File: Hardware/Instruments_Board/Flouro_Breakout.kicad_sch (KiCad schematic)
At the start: 11 parts

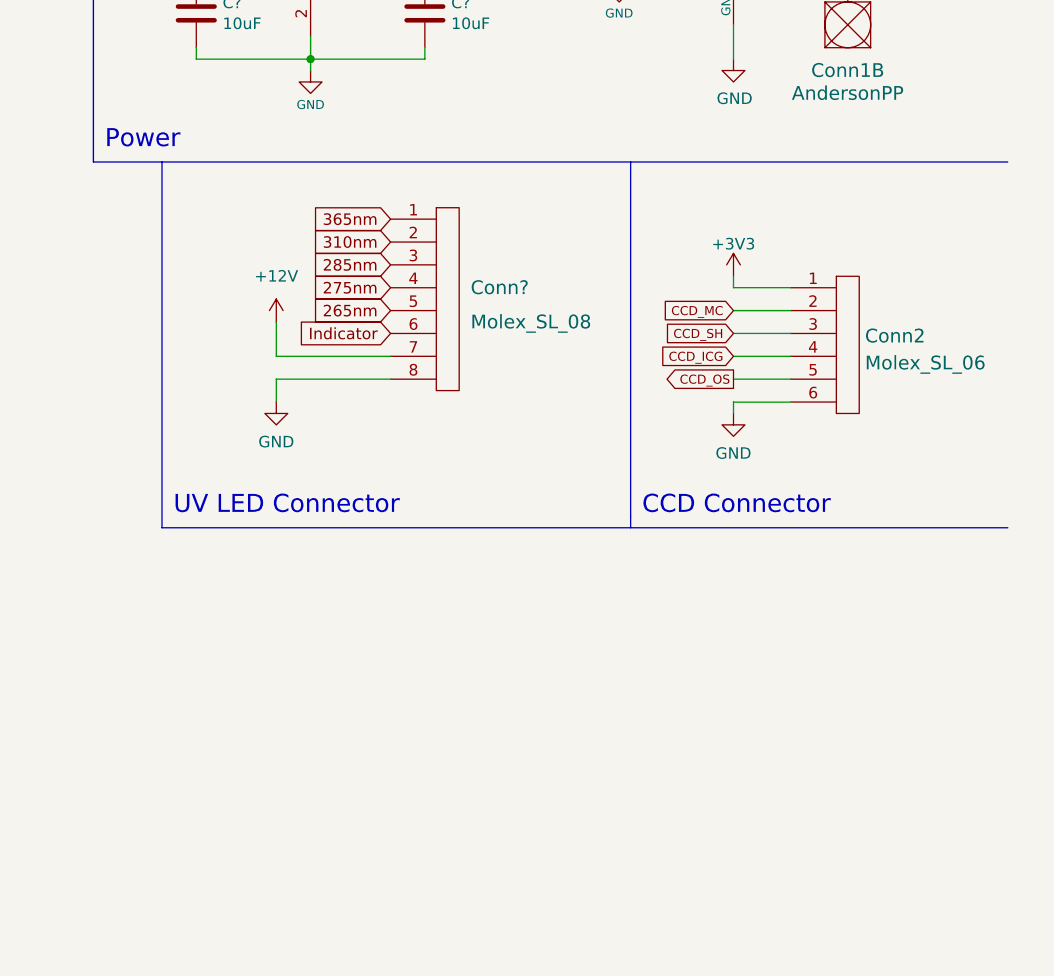
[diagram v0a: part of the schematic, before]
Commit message: New LED Footprints Made
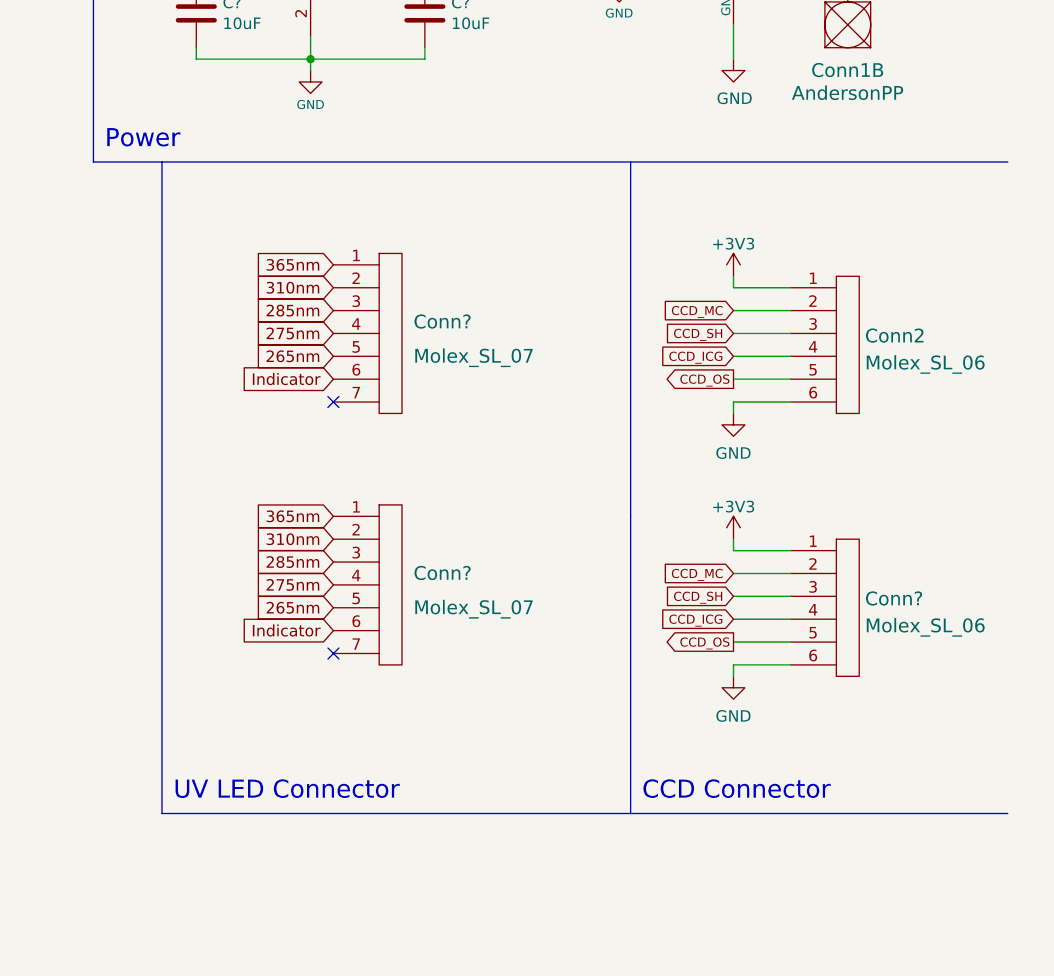
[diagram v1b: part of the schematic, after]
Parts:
- removed Conn?: Molex_SL_08, symbol MRDT_Connectors:Molex_SL_08
- added Conn? (x2): Molex_SL_07, symbol MRDT_Connectors:Molex_SL_07
- added Conn?: Molex_SL_06, Connector_Molex:Molex_SL_171971-0006_1x06_P2.54mm_Vertical, symbol Molex_SL_06:Molex_SL_06
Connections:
- net +3V3: now also Conn?.1
- net 265nm: now also Conn?.5, Conn?.5
- net 275nm: now also Conn?.4, Conn?.4
- net 285nm: now also Conn?.3, Conn?.3
- net 310nm: now also Conn?.2, Conn?.2
- net 365nm: now also Conn?.1, Conn?.1
- net CCD_ICG: now also Conn?.4
- net CCD_MC: now also Conn?.2
- net CCD_OS: now also Conn?.5
- net CCD_SH: now also Conn?.3
- net GND: now also Conn?.6
- net Indicator: now also Conn?.6, Conn?.6
- no-connect marks 3 -> 5

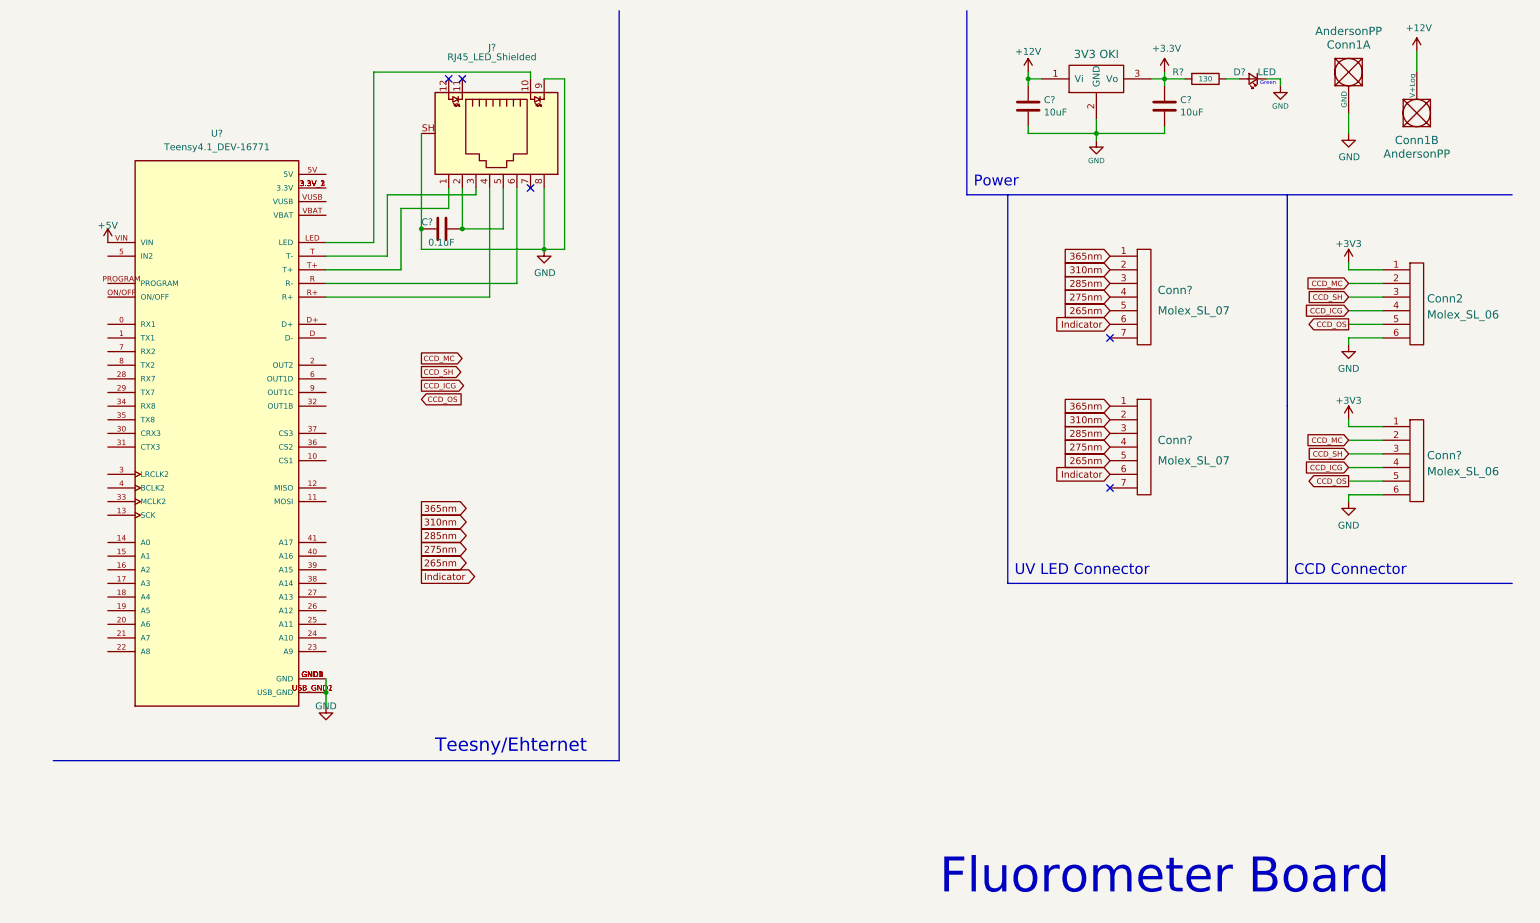
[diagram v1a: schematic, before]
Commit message: Began future proofing instruments board
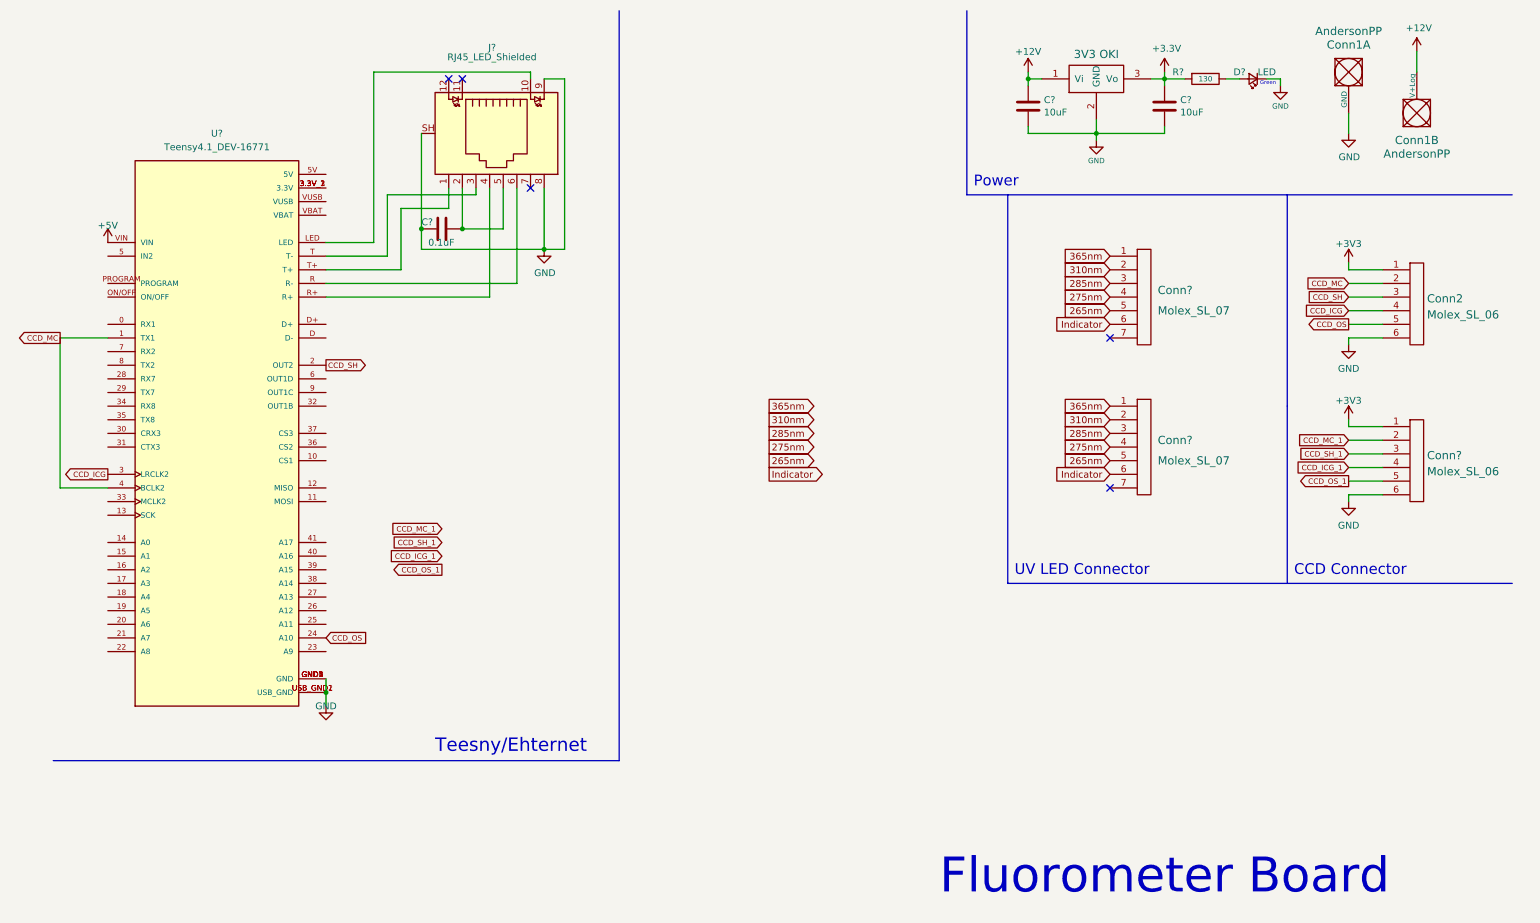
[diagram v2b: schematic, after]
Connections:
- net CCD_ICG: now also U?.3 (LRCLK2); no longer Conn?.4
- net CCD_MC: now also U?.1 (TX1), U?.4 (BCLK2); no longer Conn?.2
- net CCD_OS: now also U?.24 (A10); no longer Conn?.5
- net CCD_SH: now also U?.2 (OUT2); no longer Conn?.3
- new net  CCD_SH_1: Conn?.3
- new net CCD_ICG_1: Conn?.4
- new net CCD_MC_1: Conn?.2
- new net CCD_OS_1: Conn?.5
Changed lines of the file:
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@@
     (stroke (width 0) (type default) (color 0 0 0 0))
   )
+  (wire (pts (xy 13.97 101.6) (xy 22.86 101.6))
+    (stroke (width 0) (type default) (color 0 0 0 0))
+  )
   (wire (pts (xy 72.39 24.13) (xy 72.39 55.88))
     (stroke (width 0) (type default) (color 0 0 0 0))
@@
     (stroke (width 0) (type default) (color 0 0 0 0))
   )
+  (wire (pts (xy 22.86 73.66) (xy 13.97 73.66))
+    (stroke (width 0) (type default) (color 0 0 0 0))
+  )
   (wire (pts (xy 254 95.25) (xy 260.35 95.25))
     (stroke (width 0) (type default) (color 0 0 0 0))
@@
     (stroke (width 0) (type default) (color 0 0 0 0))
   )
+  (wire (pts (xy 13.97 73.66) (xy 13.97 101.6))
+    (stroke (width 0) (type default) (color 0 0 0 0))
+  )
   (wire (pts (xy 254 97.79) (xy 260.35 97.79))
     (stroke (width 0) (type default) (color 0 0 0 0))
@@
     (effects (font (size 2.5 2.5)) (justify left bottom))
   )
-  (global_label "Indicator" (shape output) (at 81.28 118.11 0) (fields_autoplaced)
+  (global_label "Indicator" (shape output) (at 146.05 99.06 0) (fields_autoplaced)
     (effects (font (size 1.27 1.27)) (justify left))
-    (property "Intersheet References" "${INTERSHEET_REFS}" (id 0) (at 92.0993 118.0306 0)
+    (property "Intersheet References" "${INTERSHEET_REFS}" (id 0) (at 156.8693 98.9806 0)
       (effects (font (size 1.27 1.27)) (justify left) hide)
     )
   )
+  (global_label "CCD_SH" (shape output) (at 63.5 78.74 0) (fields_autoplaced)
+    (effects (font (size 1 1)) (justify left))
+    (property "Intersheet References" "${INTERSHEET_REFS}" (id 0) (at 71.1619 78.6775 0)
+      (effects (font (size 1 1)) (justify left) hide)
+    )
+  )
+  (global_label "CCD_OS_1" (shape output) (at 85.09 116.84 180) (fields_autoplaced)
+    (effects (font (size 1 1)) (justify right))
+    (property "Intersheet References" "${INTERSHEET_REFS}" (id 0) (at 75.7138 116.7775 0)
+      (effects (font (size 1 1)) (justify right) hide)
+    )
+  )
   (global_label "CCD_OS" (shape output) (at 254 71.12 180) (fields_autoplaced)
     (effects (font (size 1 1)) (justify right))
@@
     )
   )
-  (global_label "265nm" (shape output) (at 81.28 115.57 0) (fields_autoplaced)
+  (global_label "265nm" (shape output) (at 146.05 96.52 0) (fields_autoplaced)
     (effects (font (size 1.27 1.27)) (justify left))
-    (property "Intersheet References" "${INTERSHEET_REFS}" (id 0) (at 90.1641 115.4906 0)
+    (property "Intersheet References" "${INTERSHEET_REFS}" (id 0) (at 154.9341 96.4406 0)
       (effects (font (size 1.27 1.27)) (justify left) hide)
     )
   )
-  (global_label "CCD_SH" (shape output) (at 81.28 80.01 0) (fields_autoplaced)
-    (effects (font (size 1 1)) (justify left))
-    (property "Intersheet References" "${INTERSHEET_REFS}" (id 0) (at 88.9419 79.9475 0)
-      (effects (font (size 1 1)) (justify left) hide)
-    )
-  )
   (global_label "265nm" (shape input) (at 209.55 96.52 180) (fields_autoplaced)
     (effects (font (size 1.27 1.27)) (justify right))
@@
     )
   )
-  (global_label "CCD_ICG" (shape input) (at 254 97.79 180) (fields_autoplaced)
+  (global_label "CCD_ICG_1" (shape input) (at 254 97.79 180) (fields_autoplaced)
+    (effects (font (size 1 1)) (justify right))
+    (property "Intersheet References" "${INTERSHEET_REFS}" (id 0) (at 244.1476 97.7275 0)
+      (effects (font (size 1 1)) (justify right) hide)
+    )
+  )
+  (global_label "CCD_MC_1" (shape input) (at 254 92.71 180) (fields_autoplaced)
     (effects (font (size 1 1)) (justify right))
-    (property "Intersheet References" "${INTERSHEET_REFS}" (id 0) (at 245.9319 97.7275 0)
+    (property "Intersheet References" "${INTERSHEET_REFS}" (id 0) (at 244.481 92.6475 0)
       (effects (font (size 1 1)) (justify right) hide)
     )
   )
-  (global_label "CCD_MC" (shape input) (at 254 92.71 180) (fields_autoplaced)
+  (global_label "CCD_MC" (shape output) (at 13.97 73.66 180) (fields_autoplaced)
     (effects (font (size 1 1)) (justify right))
-    (property "Intersheet References" "${INTERSHEET_REFS}" (id 0) (at 246.2652 92.6475 0)
+    (property "Intersheet References" "${INTERSHEET_REFS}" (id 0) (at 6.1652 73.7225 0)
       (effects (font (size 1 1)) (justify right) hide)
     )
   )
-  (global_label "285nm" (shape output) (at 81.28 110.49 0) (fields_autoplaced)
+  (global_label "285nm" (shape output) (at 146.05 91.44 0) (fields_autoplaced)
     (effects (font (size 1.27 1.27)) (justify left))
-    (property "Intersheet References" "${INTERSHEET_REFS}" (id 0) (at 90.1641 110.4106 0)
+    (property "Intersheet References" "${INTERSHEET_REFS}" (id 0) (at 154.9341 91.3606 0)
       (effects (font (size 1.27 1.27)) (justify left) hide)
     )
@@
     )
   )
-  (global_label "CCD_MC" (shape output) (at 81.28 77.47 0) (fields_autoplaced)
-    (effects (font (size 1 1)) (justify left))
-    (property "Intersheet References" "${INTERSHEET_REFS}" (id 0) (at 89.0848 77.4075 0)
-      (effects (font (size 1 1)) (justify left) hide)
+  (global_label " CCD_SH_1" (shape input) (at 85.09 111.76 180) (fields_autoplaced)
+    (effects (font (size 1 1)) (justify right))
+    (property "Intersheet References" "${INTERSHEET_REFS}" (id 0) (at 74.9519 111.6975 0)
+      (effects (font (size 1 1)) (justify right) hide)
     )
   )
@@
     )
   )
-  (global_label "365nm" (shape output) (at 81.28 105.41 0) (fields_autoplaced)
+  (global_label "365nm" (shape output) (at 146.05 86.36 0) (fields_autoplaced)
     (effects (font (size 1.27 1.27)) (justify left))
-    (property "Intersheet References" "${INTERSHEET_REFS}" (id 0) (at 90.1641 105.3306 0)
+    (property "Intersheet References" "${INTERSHEET_REFS}" (id 0) (at 154.9341 86.2806 0)
       (effects (font (size 1.27 1.27)) (justify left) hide)
     )
@@
     )
   )
-  (global_label "CCD_OS" (shape input) (at 81.28 85.09 0) (fields_autoplaced)
-    (effects (font (size 1 1)) (justify left))
-    (property "Intersheet References" "${INTERSHEET_REFS}" (id 0) (at 88.9419 85.0275 0)
-      (effects (font (size 1 1)) (justify left) hide)
-    )
-  )
   (global_label "Indicator" (shape input) (at 209.55 99.06 180) (fields_autoplaced)
     (effects (font (size 1.27 1.27)) (justify right))
@@
     )
   )
+  (global_label "CCD_MC_1" (shape input) (at 85.09 109.22 180) (fields_autoplaced)
+    (effects (font (size 1 1)) (justify right))
+    (property "Intersheet References" "${INTERSHEET_REFS}" (id 0) (at 75.571 109.1575 0)
+      (effects (font (size 1 1)) (justify right) hide)
+    )
+  )
   (global_label "365nm" (shape input) (at 209.55 86.36 180) (fields_autoplaced)
     (effects (font (size 1.27 1.27)) (justify right))
@@
     )
   )
-  (global_label "CCD_ICG" (shape output) (at 81.28 82.55 0) (fields_autoplaced)
-    (effects (font (size 1 1)) (justify left))
-    (property "Intersheet References" "${INTERSHEET_REFS}" (id 0) (at 89.4181 82.4875 0)
-      (effects (font (size 1 1)) (justify left) hide)
-    )
-  )
-  (global_label "275nm" (shape output) (at 81.28 113.03 0) (fields_autoplaced)
+  (global_label "275nm" (shape output) (at 146.05 93.98 0) (fields_autoplaced)
     (effects (font (size 1.27 1.27)) (justify left))
-    (property "Intersheet References" "${INTERSHEET_REFS}" (id 0) (at 90.1641 112.9506 0)
+    (property "Intersheet References" "${INTERSHEET_REFS}" (id 0) (at 154.9341 93.9006 0)
       (effects (font (size 1.27 1.27)) (justify left) hide)
     )
   )
+  (global_label "CCD_ICG" (shape output) (at 22.86 99.06 180) (fields_autoplaced)
+    (effects (font (size 1 1)) (justify right))
+    (property "Intersheet References" "${INTERSHEET_REFS}" (id 0) (at 14.7219 99.1225 0)
+      (effects (font (size 1 1)) (justify right) hide)
+    )
+  )
   (global_label "365nm" (shape input) (at 209.55 58.42 180) (fields_autoplaced)
     (effects (font (size 1.27 1.27)) (justify right))
@@
     )
   )
-  (global_label "310nm" (shape output) (at 81.28 107.95 0) (fields_autoplaced)
+  (global_label "310nm" (shape output) (at 146.05 88.9 0) (fields_autoplaced)
     (effects (font (size 1.27 1.27)) (justify left))
-    (property "Intersheet References" "${INTERSHEET_REFS}" (id 0) (at 90.1641 107.8706 0)
+    (property "Intersheet References" "${INTERSHEET_REFS}" (id 0) (at 154.9341 88.8206 0)
       (effects (font (size 1.27 1.27)) (justify left) hide)
     )
   )
-  (global_label "CCD_OS" (shape output) (at 254 100.33 180) (fields_autoplaced)
+  (global_label "CCD_OS_1" (shape output) (at 254 100.33 180) (fields_autoplaced)
     (effects (font (size 1 1)) (justify right))
-    (property "Intersheet References" "${INTERSHEET_REFS}" (id 0) (at 246.4081 100.2675 0)
+    (property "Intersheet References" "${INTERSHEET_REFS}" (id 0) (at 244.6238 100.2675 0)
       (effects (font (size 1 1)) (justify right) hide)
     )
@@
     )
   )
-  (global_label "CCD_SH" (shape input) (at 254 95.25 180) (fields_autoplaced)
+  (global_label " CCD_SH_1" (shape input) (at 254 95.25 180) (fields_autoplaced)
     (effects (font (size 1 1)) (justify right))
-    (property "Intersheet References" "${INTERSHEET_REFS}" (id 0) (at 246.4081 95.1875 0)
+    (property "Intersheet References" "${INTERSHEET_REFS}" (id 0) (at 243.8619 95.1875 0)
       (effects (font (size 1 1)) (justify right) hide)
     )
   )
+  (global_label "CCD_OS" (shape input) (at 63.5 129.54 0) (fields_autoplaced)
+    (effects (font (size 1 1)) (justify left))
+    (property "Intersheet References" "${INTERSHEET_REFS}" (id 0) (at 71.1619 129.4775 0)
+      (effects (font (size 1 1)) (justify left) hide)
+    )
+  )
   (global_label "CCD_MC" (shape input) (at 254 63.5 180) (fields_autoplaced)
     (effects (font (size 1 1)) (justify right))
@@
       (effects (font (size 1 1)) (justify right) hide)
     )
+  )
+  (global_label "CCD_ICG_1" (shape input) (at 85.09 114.3 180) (fields_autoplaced)
+    (effects (font (size 1 1)) (justify right))
+    (property "Intersheet References" "${INTERSHEET_REFS}" (id 0) (at 75.2376 114.2375 0)
+      (effects (font (size 1 1)) (justify right) hide)
+    )

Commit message: I Forgot
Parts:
- removed Conn? (x2): Molex_SL_07, symbol MRDT_Connectors:Molex_SL_07
- added Conn?: Molex_SL_07, MRDT_Connectors:MOLEX_SL_07_Vertical, symbol MRDT_Connectors:Molex_SL_07
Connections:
- net  CCD_SH_1: now also U?.6 (OUT1D)
- net +12V: now also Conn?.1
- net 275nm: now also U?.38 (A14), Conn?.5
- net 310nm: now also U?.40 (A16), Conn?.3
- net 365nm: now also U?.41 (A17), Conn?.2
- net CCD_ICG_1: now also U?.7 (RX2)
- net CCD_MC_1: now also U?.5 (IN2), U?.8 (TX2)
- net CCD_OS_1: now also U?.25 (A11)
- net GND: now also Conn?.7
- net 260nm: now reaches U?.27 (A13)
- net 260nm: now also Conn?.6
- net 280nm: now reaches U?.39 (A15)
- net 280nm: now also Conn?.4
- no-connect marks 5 -> 3
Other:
- note added: "CCD Conn"
- note added: "CCD Conn_1"
- note added: "CCD Connectors"
- note removed: "CCD Connector"
- moved on the sheet: C?, Conn2, Conn?, J?, U?

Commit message: Fixed things grant suggested
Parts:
- R1: renamed from R?; value 130 -> 100
- U1: renamed from U?; footprint MODULE_DEV-16771 -> MRDT_Shields:Teensy_4_1
- gave numbers to parts that had none: 8
